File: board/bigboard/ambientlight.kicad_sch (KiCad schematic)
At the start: 2 parts, among them U10 APDS-9306-065

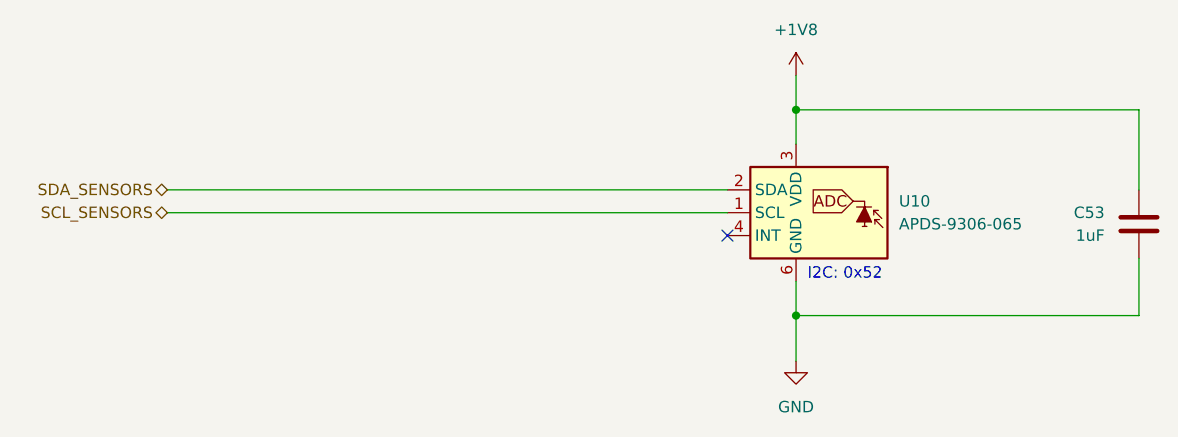
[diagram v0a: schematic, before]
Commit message: Manufactured version of bigboard
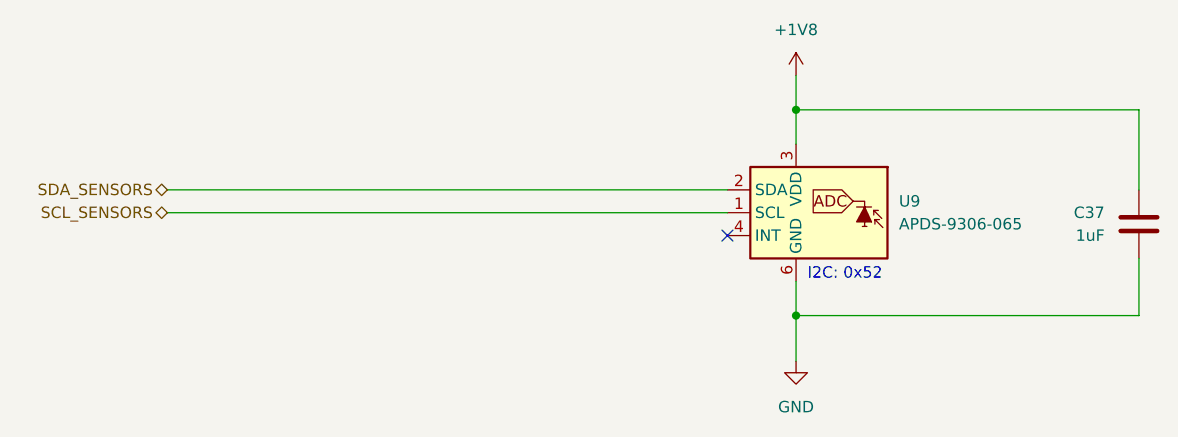
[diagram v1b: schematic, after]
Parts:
- C37: renamed from C53; MPN (none) -> CC0201MRX5R6BB105
- renumbered U10 to U9
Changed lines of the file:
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@@
   (symbol (lib_id "Sensor_Optical:APDS-9306-065") (at 140.97 97.79 0) (mirror y) (unit 1)
     (in_bom yes) (on_board yes) (fields_autoplaced)
-    (property "Reference" "U10" (id 0) (at 149.86 96.5199 0)
+    (property "Reference" "U9" (id 0) (at 149.86 96.5199 0)
       (effects (font (size 1.27 1.27)) (justify right))
     )
@@
   (symbol (lib_id "Device:C") (at 176.53 99.06 0) (mirror y) (unit 1)
     (in_bom yes) (on_board yes) (fields_autoplaced)
-    (property "Reference" "C53" (id 0) (at 172.72 97.7899 0)
+    (property "Reference" "C37" (id 0) (at 172.72 97.7899 0)
       (effects (font (size 1.27 1.27)) (justify left))
     )
@@
       (effects (font (size 1.27 1.27)) hide)
     )
-    (property "Description" "CAP CERM 1uF +/10% 25V X5R 0201" (id 4) (at 176.53 99.06 0)
+    (property "Description" "CAP CERM 1uF +/20% 10V X5R 0201" (id 4) (at 176.53 99.06 0)
+      (effects (font (size 1.27 1.27)) hide)
+    )
+    (property "MPN" "CC0201MRX5R6BB105" (id 5) (at 176.53 99.06 0)
       (effects (font (size 1.27 1.27)) hide)
     )
@@
   (symbol (lib_id "power:GND") (at 138.43 114.3 0) (mirror y) (unit 1)
     (in_bom yes) (on_board yes) (fields_autoplaced)
-    (property "Reference" "#PWR042" (id 0) (at 138.43 120.65 0)
+    (property "Reference" "#PWR038" (id 0) (at 138.43 120.65 0)
       (effects (font (size 1.27 1.27)) hide)
     )
@@
   (symbol (lib_id "power:+1V8") (at 138.43 82.55 0) (mirror y) (unit 1)
     (in_bom yes) (on_board yes) (fields_autoplaced)
-    (property "Reference" "#PWR041" (id 0) (at 138.43 86.36 0)
+    (property "Reference" "#PWR037" (id 0) (at 138.43 86.36 0)
       (effects (font (size 1.27 1.27)) hide)
     )
